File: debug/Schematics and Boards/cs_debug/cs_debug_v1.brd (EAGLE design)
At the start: 38.1 x 44.5 mm, 131 parts, among them J401 J-USB-HIROSE-MICRO-USB, Q10 2N7002P, Q3 FDN340P, Q4 2N7002P, Q5 FDN340P, Q6 2N7002P, Q7 FDN340P, Q8 2N7002P, Q9 FDN340P, U1 AP2120N-3.3TRG1, U10 OPA357AIDBVTG4, U2 TLV1117LV33DCYR, U3 INA225AIDGK, U4 OPA357AIDBVTG4, U5 INA225AIDGK, U6 OPA357AIDBVTG4, U7 INA225AIDGK, U8 OPA357AIDBVTG4, U9 INA225AIDGK, Y101 32.768kHz, Y102 12mHz-12pF-K7

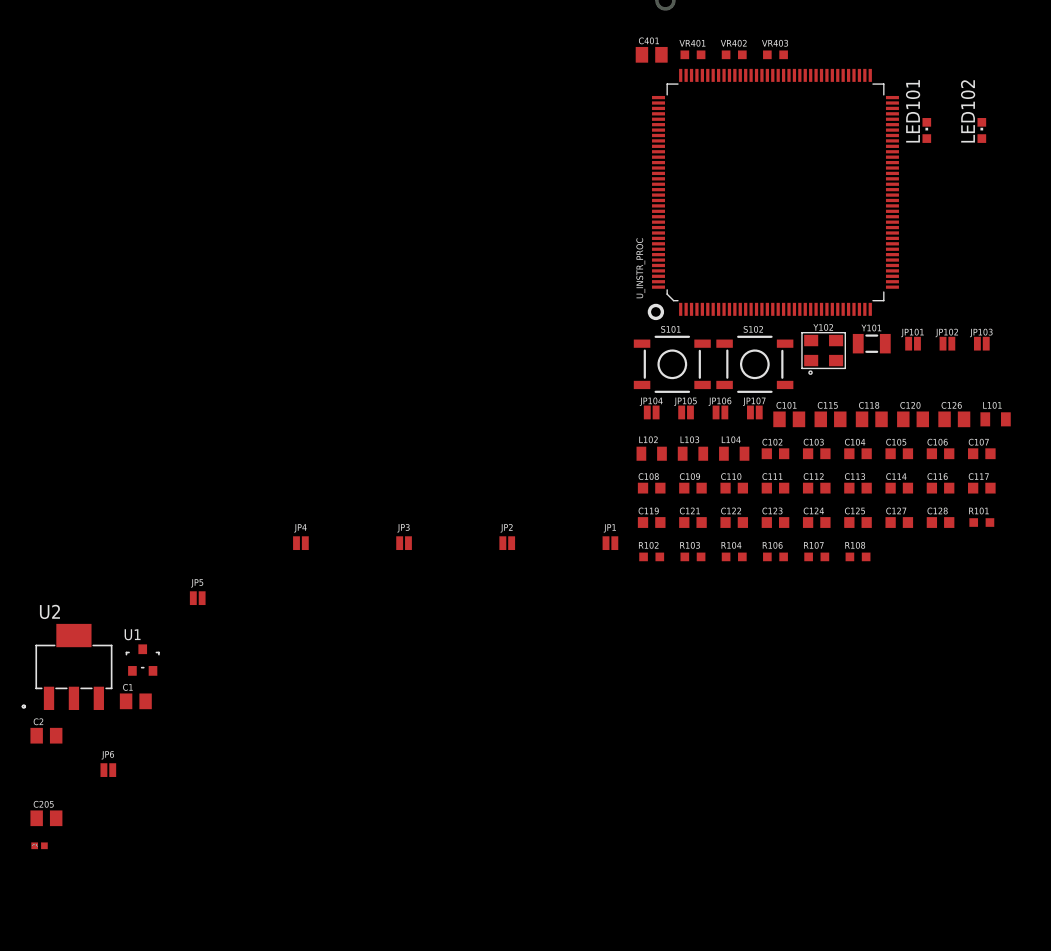
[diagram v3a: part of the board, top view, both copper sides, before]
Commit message: Signals from instrumentation processor to current monitors
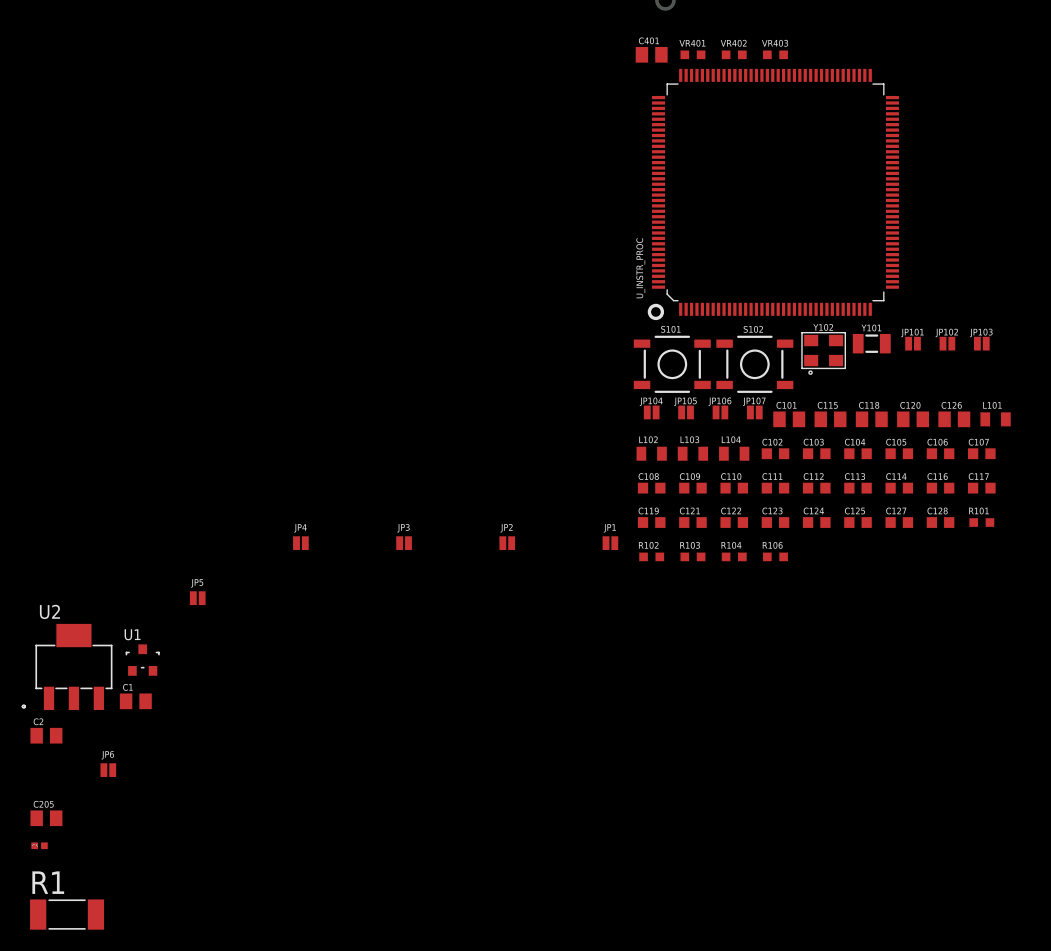
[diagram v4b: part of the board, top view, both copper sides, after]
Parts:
- removed LED101: RED, adafruit:CHIPLED_0603
- removed LED102: GREEN, adafruit:CHIPLED_0603
- removed R107, R108: 1k, Resistors:R0603
- added R1: 0, Resistors:R2010
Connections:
- net D+ renamed INSTR_PROC_USB_D_P
- net D- renamed INSTR_PROC_USB_D_N
- net MAIN_TRACE_D2 renamed MAIN_TRACE_D2/GPIO8
- net MAIN_TRACE_D3 renamed MAIN_TRACE_D3/GPIO9
- removed net CM_PROC_V_OFFSET_IN: R9.1
- removed net MAIN_TRACE_CLK: J_DEBUG_TO_MAIN_HEADER.26
- removed net MAIN_TRACE_D0: J_DEBUG_TO_MAIN_HEADER.23
- removed net MAIN_TRACE_D1: J_DEBUG_TO_MAIN_HEADER.25
- removed net MAIN_TRACE_SWO: J_DEBUG_TO_MAIN_HEADER.28
- removed net N$31: LED101.A, R107.1
- removed net USR_LED_GREEN: LED102.C
- removed net USR_LED_RED: LED101.C
- new net INSTR_PROC_USART_RX: U_INSTR_PROC.18
- new net INSTR_PROC_USART_TX: U_INSTR_PROC.17
- new net MAIN_TRACE_CLK/GPIO4: J_DEBUG_TO_MAIN_HEADER.26, U_INSTR_PROC.97
- new net MAIN_TRACE_D0/GPIO6: J_DEBUG_TO_MAIN_HEADER.23, U_INSTR_PROC.114
- new net MAIN_TRACE_D1/GPIO7: J_DEBUG_TO_MAIN_HEADER.25, U_INSTR_PROC.115
- new net MAIN_TRACE_SWO/GPIO5: J_DEBUG_TO_MAIN_HEADER.28, U_INSTR_PROC.113
- new net N$10: U_INSTR_PROC.87
- new net N$11: U_INSTR_PROC.85
- net 3V3_INSTR_PROC: no longer R107.2, R108.2
- net AGND: now also R1.2
- net CM_DTR_DCBIAS_SHUTDOWN: now also U_INSTR_PROC.15
- net CM_DTR_DIFFAMP_GAIN0: now also U_INSTR_PROC.64
- net CM_DTR_DIFFAMP_GAIN1: now also U_INSTR_PROC.63
- net CM_DTR_DIFFAMP_OUT: now also U_INSTR_PROC.82
- net CM_PROC_DCBIAS_SHUTDOWN: now also U_INSTR_PROC.16
- net CM_PROC_DIFFAMP_GAIN0: now also U_INSTR_PROC.66
- net CM_PROC_DIFFAMP_GAIN1: now also U_INSTR_PROC.65
- net CM_PROC_DIFFAMP_OUT: now also U_INSTR_PROC.78
- net CM_STORAGE_DCBIAS_SHUTDOWN: now also U_INSTR_PROC.14
- net CM_STORAGE_DIFFAMP_GAIN0: now also U_INSTR_PROC.116
- net CM_STORAGE_DIFFAMP_GAIN1: now also U_INSTR_PROC.60
- net CM_STORAGE_DIFFAMP_OUT: now also U_INSTR_PROC.83
- net CM_TEMP_DCBIAS_SHUTDOWN: now also U_INSTR_PROC.13
- net CM_TEMP_DIFFAMP_GAIN0: now also U_INSTR_PROC.59
- net CM_TEMP_DIFFAMP_GAIN1: now also U_INSTR_PROC.55
- net CM_TEMP_DIFFAMP_OUT: now also U_INSTR_PROC.84
- net DGND: now also R1.1
- net MAIN_GPIO0: now also U_INSTR_PROC.101
- net MAIN_GPIO1: now also U_INSTR_PROC.100
- net MAIN_GPIO2: now also U_INSTR_PROC.99
- net MAIN_GPIO3: now also U_INSTR_PROC.98
- net N$3: now also U_INSTR_PROC.129; no longer C205.1, C3.1, JP5.1, JP6.1
- net N$5: now also U_INSTR_PROC.86; no longer LED102.A, R108.1
- net VDD_TO_MAIN: now also C205.1, C3.1, JP5.1, JP6.1

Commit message: Add debug connectors, DAC, pull-ups to schematic
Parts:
- added C16: 0.1u, Capacitors:C0402
- added J1, J2: J-JTAG-CORTEX_SMD, Connectors:SAMTECH_FTSH-105-01
- added J3: J-JTAG-CORTEX-NEEDLE6-LEGS, Connectors:8.06.16_6-PIN_NEEDLE_ADAPTER_LEGS
- added JP7: JUMPER-SMT_2_NC_PASTE_NO-SILK, SparkFun-Jumpers:SMT-JUMPER_2_NC_PASTE_NO-SILK
- added R2, R3, R6: 100k, Resistors:R0402
- added R4, R5: 4.7k, Resistors:R0402
- added U11: DAC7574IDGS, DACs:DGS10
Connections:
- removed net CPU_RESET: C119.2, S101.3, S101.4, U_INSTR_PROC.47
- removed net N$10: U_INSTR_PROC.87
- removed net N$3: U_INSTR_PROC.129
- removed net N$5: U_INSTR_PROC.86
- removed net N$6: U_INSTR_PROC.28
- removed net N$7: U_INSTR_PROC.29
- removed net N$8: U_INSTR_PROC.30
- removed net N$9: U_INSTR_PROC.31
- removed net UOTGID: J401.USBID, VR401.1
- new net CM_PROC_V_OFFSET_IN: U11.1
- new net INSTR_PROC_I2C_SCL: R4.2, U11.6, U_INSTR_PROC.87
- new net INSTR_PROC_I2C_SDA: R5.2, U11.7, U_INSTR_PROC.86
- new net INSTR_PROC_JTAG_TCK/SWCLK: J2.4, J3.4, R3.1, U_INSTR_PROC.28
- new net INSTR_PROC_JTAG_TDI: J2.8, R6.1, U_INSTR_PROC.29
- new net INSTR_PROC_JTAG_TDO/SWO: J2.6, J3.6, U_INSTR_PROC.30
- new net INSTR_PROC_JTAG_TMS/SWDIO: J2.2, J3.2, R2.1, U_INSTR_PROC.31
- new net INSTR_PROC_NRESET: C119.2, J2.10, J3.3, S101.3, S101.4, U_INSTR_PROC.47
- new net INSTR_PROC_USB_UOTGID: J401.USBID, U_INSTR_PROC.129, VR401.1
- new net N$12: C205.1, C3.1, JP5.1, JP6.1, JP7.1
- net 3V3_INSTR_MEAS: now also C16.1, U11.8
- net 3V3_INSTR_PROC: now also J2.1, J3.1, R2.2, R3.2, R4.1, R5.1, R6.2
- net AGND: now also C16.2, U11.10, U11.3, U11.9
- net CM_DTR_V_OFFSET_IN: now also U11.2
- net CM_STORAGE_V_OFFSET_IN: now also U11.4
- net CM_TEMP_V_OFFSET_IN: now also U11.5
- net DGND: now also J1.3, J1.5, J2.3, J2.5, J2.9, J3.5
- net MAIN_NRESET: now also J1.10
- net MAIN_SWD_SWCLK: now also J1.4
- net MAIN_SWD_SWDIO: now also J1.2
- net VDD_TO_MAIN: now also JP7.2; no longer C205.1, C3.1, JP5.1, JP6.1
- net V_SENSE_P: now also J1.1

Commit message: Finish first-pass of Debug Board schematic
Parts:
- removed C101, C115, C118, C120, C126: 22uF, Capacitors:C0805
- removed C102, C106: 16pF, Capacitors:C0603
- removed C104, C105, C109, C110, C111, C112, C113, C114, C116, C117, C121, C122, C123, C124, C125, C127, C128: 0.1uF, Capacitors:C0603
- removed C119: 10nF, Capacitors:C0603
- removed R104, R106: 100k, Resistors:R0603
- removed S101: Momentary, Switches:TACTILE_SWITCH_SMD_5.2MM
- added C17, C19: 16pF, Capacitors:C0603
- added C18, C208: 4.7u, Capacitors:C0402
- added C20, C28: 10n, Capacitors:C0402
- added C21, C23, C24, C25, C26, C27: 22u, Capacitors:C0805
- added C22, C29, C30, C31, C32, C33, C34, C35, C36, C37, C38, C39, C40, C41, C42, C43, C44: 0.1u, Capacitors:C0402
- added D1: MBR120VLSFT3GOSCT-ND, adafruit:SOD-123
- added F2: MF-MSMF050-2, adafruit:1812
- added J19: Solar, Connectors:JST-PH-2-SMT-RA
- added JMP_LOG: (no value), Connectors:1X03
- added JP10: JUMPER-SMT_2_NC_PASTE_NO-SILK, SparkFun-Jumpers:SMT-JUMPER_2_NC_PASTE_NO-SILK
- added JP11: JUMPER-SMT_3_1-NC_PASTE_NO-SILK, Connectors:SMT-JUMPER_3_1-NC_PASTE_NO-SILK
- added JP12, JP8, JP9: JUMPER-SMT_2_NC_PASTE_NO-SILK, Connectors:SMT-JUMPER_2_NC_PASTE_NO-SILK
- added L1: 3.3µH/±20%/450mA, SparkFun-Coils:0805
- added R201: 270k, Resistors:R0402
- added R202, R204, R41, R8: 100k, Resistors:R0402
- added R203: 2k, Resistors:R0402
- added R206, R7: 10k, Resistors:R0402
- added S1: Momentary, Switches:SW_EVQ-P7L01P
- added S201: (no value), Switches:SWITCH_SPST_SMD_A
- added U12: MCP73871T-2CCI/ML, Chargers:QFN50P400X400X100-21N
- C401: device Capacitors:C0805 -> Capacitors:C0402
- R101, R102, R103: device Resistors:R0603 -> Resistors:R0402
- S102: device Switches:TACTILE_SWITCH_SMD_5.2MM -> Switches:SW_EVQ-P7L01P
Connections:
- removed net INSTR_PROC_USART_RX: U_INSTR_PROC.18
- removed net INSTR_PROC_USART_TX: U_INSTR_PROC.17
- removed net N$12: C205.1, C3.1, JP5.1, JP6.1, JP7.1
- removed net VUSB: C401.1, J401.VBUS
- new net BAT_CHG_PROG1: R203.2, U12.13
- new net CHG_VPCC: R201.1, R202.2, U12.2
- new net EXT_VIN: D1.A, J19.1
- new net GND: C18.2, C208.2, J19.2, S1.1_1, S1.1_2
- new net INSTR_PROC_NRESET_SW: C28.2, JP12.2, S1.2_1, S1.2_2, U_INSTR_PROC.47
- new net N$10: R204.2, U12.12
- new net N$3: JP8.2, U_INSTR_PROC.18
- new net N$5: JP9.2, U_INSTR_PROC.17
- new net N$6: L1.2, S201.2
- new net N$8: F2.2, U12.14, U12.15, U12.16
- new net THERM: R206.2, U12.5
- new net VCHRG_BATT: C18.1, F2.1, JP10.1
- new net VCHRG_OUT: C208.1, JP11.3, U12.1, U12.20
- new net VREG_IN: C205.1, C3.1, JP11.2, JP5.1, JP6.1, JP7.1
- new net VSRC_RAW: JP11.1, R201.2, S201.3, U12.17, U12.18, U12.19, U12.3, U12.4, U12.9
- net 3V3_INSTR_PROC: now also C27.1, C28.1, C37.1, C38.1, C39.1, C40.1, C41.1, C42.1, R41.1, S102.1_1, S102.1_2; no longer C101.1, C104.1, C105.1, C109.1, C110.1, C111.1, C112.1, C119.1, R106.2, S102.1, S102.2
- net ADVREF: now also C29.1; no longer C116.1
- net ADVREF_PRE: now also C22.1; no longer C114.1
- net CM_PROC_V_OFFSET_IN: now also R9.1
- net DGND: now also C17.2, C19.2, C20.2, C21.2, C22.2, C23.2, C24.2, C25.2, C26.2, C27.2, C29.2, C30.2, C31.2, C32.2, C33.2, C34.2, C35.2, C36.2, C37.2, C38.2, C39.2, C40.2, C41.2, C42.2, C43.2, C44.2, JMP_LOG.3, R202.1, R203.1, R204.1, R206.1, R7.1, R8.2, U12.10, U12.11, U12.21; no longer C101.2, C102.2, C104.2, C105.2, C106.2, C109.2, C110.2, C111.2, C112.2, C113.2, C114.2, C115.2, C116.2, C117.2, C118.2, C120.2, C121.2, C122.2, C123.2, C124.2, C125.2, C126.2, C127.2, C128.2, R104.1, S101.1, S101.2
- net ERASE_S: now also S102.2_1, S102.2_2; no longer S102.3, S102.4
- net FWUP: now also R41.2; no longer R106.1
- net INSTR_PROC_NRESET: now also JP12.1; no longer C119.2, S101.3, S101.4, U_INSTR_PROC.47
- net MAIN_USART_RX: now also JMP_LOG.1, JP8.1
- net MAIN_USART_TX: now also JMP_LOG.2, JP9.1
- net TST: now also R8.1; no longer R104.2
- net VBUS: now also C20.1, C21.1, C401.1, D1.C, J401.VBUS, L1.1, R7.2
- net VDDANA1: now also C25.1, C44.1; no longer C117.1, C118.1
- net VDDOUT: now also C23.1, C30.1, C31.1, C32.1, C33.1, C34.1, C35.1; no longer C120.1, C121.1, C122.1, C123.1, C125.1, C127.1, C128.1
- net VDDOUTMI: now also C26.1, C43.1; no longer C113.1, C115.1
- net VDDPLL: now also C24.1, C36.1; no longer C124.1, C126.1
- net V_BATT_MAIN: now also JP10.2
- net XIN: now also C19.1; no longer C106.1
- net XOUT: now also C17.1; no longer C102.1

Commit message: Change USART Header on debug board
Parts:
- removed JMP_LOG: (no value), Connectors:1X03
- added C45: 2.2uF, Capacitors:C0805
- added J4: J-SERIAL-PORT, Connectors:HEADER-1X6
- added J403: J-WURTH-USBC, Connectors:632723X00011
- added JP13: JUMPER-SMT_2_NC_PASTE_NO-SILK, Connectors:SMT-JUMPER_2_NC_PASTE_NO-SILK
- added R422, R423: 5.1k, Resistors:R0603
- added VR1, VR2: VARISTOR, Diodes:R0603
- moved R33 2.54 mm to (57.1, -48.9)
- moved R34 2.54 mm to (59.7, -48.9)
- moved R35 2.54 mm to (62.2, -48.9)
- moved R36 2.54 mm to (64.8, -48.9)
- moved R37 2.54 mm to (67.3, -48.9)
- moved C13 2.54 mm to (62.2, -46.4)
- moved C14 2.54 mm to (64.8, -46.4)
- moved C15 2.54 mm to (67.3, -46.4)
- moved Q10 2.54 mm to (58.4, -41.3)
- moved Q9 2.54 mm to (58.4, -36.2)
- moved R38 2.54 mm to (57.1, -51.4)
- moved R39 2.54 mm to (67.3, -40.0)
- moved R40 2.54 mm to (58.4, -46.4)
- moved U10 2.54 mm to (63.5, -42.5)
- moved U9 2.54 mm to (64.8, -36.2)
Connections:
- new net CC1: J403.A5, R422.2
- new net CC2: J403.B5, R423.2
- new net D+: J403.A6, J403.B6, VR1.1
- new net D-: J403.A7, J403.B7, VR2.1
- new net UCTX_DBGRX: J403.A8, J403.B8
- net 3V3_INSTR_PROC: now also JP13.1
- net DGND: now also J4.1; no longer JMP_LOG.3
- net GND: now also C45.2, J403.A1, J403.A12, J403.B1, J403.B12, J403.GND, J403.GND1, J403.Z1, J403.Z2, J403.Z3, J403.Z4, J403.Z5, J403.Z6, R422.1, R423.1, VR1.2, VR2.2
- net MAIN_USART_RX: now also J4.5; no longer JMP_LOG.1
- net MAIN_USART_TX: now also J4.4; no longer JMP_LOG.2
- net N$11: now also J4.3, JP13.2; no longer U_INSTR_PROC.85
- net VBUS: now also C45.1, J403.A4, J403.A9, J403.B4, J403.B9

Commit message: Add USB connector and switch IC
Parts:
- removed C20: 10n, Capacitors:C0402
- removed C21: 22u, Capacitors:C0805
- removed C401: 2.2uF, Capacitors:C0402
- removed C45: 2.2uF, Capacitors:C0805
- removed J401: J-USB-HIROSE-MICRO-USB, Connectors:USB-THRU-ZX62D-AB-5P8
- removed J403: J-WURTH-USBC, Connectors:632723X00011
- removed R422, R423: 5.1k, Resistors:R0603
- removed R7: 10k, Resistors:R0402
- removed VR1, VR2, VR401, VR402, VR403: VARISTOR, Diodes:R0603
- added C46: 2.2uF, Capacitors:C0805
- added C47: 1u, Capacitors:C0402
- added C48, C49, C50, C51, C52, C53: 0.1u, Capacitors:C0402
- added C54: 4.7u, Capacitors:C0402
- added C55, C56: 18pF, Capacitors:C0402
- added J5: J-WURTH-USBC, Connectors:632723X00011
- added JP14, JP15, JP16: JUMPER-SMT_2_NC_PASTE_NO-SILK, SparkFun-Jumpers:SMT-JUMPER_2_NC_PASTE_NO-SILK
- added L2: DLP11SN900HL2L, Inductors:IND_DLP11S_0504_MUR
- added R42, R43: 5.1k, Resistors:R0603
- added R44, R45, R51, R52: 10k, Resistors:R0402
- added R46, R47, R49, R50: 100k, Resistors:R0402
- added R48: 12k, Resistors:R0402
- added U$5: BGX50A, Diodes:SOT143_BGX50A
- added U13: USB2412-DZK, Switches:QFN28_5X5MC_MCH
- added VR3, VR4: VARISTOR, Diodes:R0603
- added Y1: HCM49-24.000MABJ-UT, Oscillators:XTAL_HCM49
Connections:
- removed net CC1: J403.A5, R422.2
- removed net CC2: J403.B5, R423.2
- removed net D+: J403.A6, J403.B6, VR1.1
- removed net D-: J403.A7, J403.B7, VR2.1
- removed net VBUS: C20.1, C21.1, C401.1, C45.1, D1.C, J401.VBUS, J403.A4, J403.A9, J403.B4, J403.B9, L1.1, R7.2, U_INSTR_PROC.39
- new net CC3: J5.A5, R42.2
- new net CC4: J5.B5, R43.2
- new net N$12: U13.15, U13.6
- new net N$14: R45.1, U13.7
- new net N$15: D1.C, JP14.1
- new net N$16: R44.1, U13.11
- new net N$17: R48.2, U13.26
- new net N$18: R46.2, R47.1, U13.18
- new net N$19: C48.1, R49.1, U13.17
- new net N$20: C55.1, U13.24, Y1.1
- new net N$21: C56.1, U13.23, Y1.2
- new net N$22: R50.2, U13.16
- new net N$23: R52.1, U13.13
- new net N$24: R51.1, U13.19
- new net USB_CONN_D_N: J5.A6, J5.B6, L2.3, U$5.2, VR3.1
- new net USB_CONN_D_P: J5.A7, J5.B7, L2.2, U$5.4, VR4.1
- new net USB_D_N: L2.4, U13.21
- new net USB_D_P: L2.1, U13.22
- new net USB_VBUS: C46.1, C47.1, J5.A4, J5.A9, J5.B4, J5.B9, JP14.2, JP15.1, JP15.2, L1.1, R47.2, U$5.1, U_INSTR_PROC.39
- net 3V3_INSTR_PROC: now also C49.1, C50.1, C51.1, C52.1, C53.1, C54.1, R44.2, R45.2, R49.2, R51.2, R52.2, U13.10, U13.14, U13.20, U13.27, U13.4
- net DGND: now also C46.2, C47.2, C48.2, C49.2, C50.2, C51.2, C52.2, C53.2, C54.2, C55.2, C56.2, J5.A1, J5.A12, J5.B1, J5.B12, J5.GND, J5.GND1, J5.Z1, J5.Z2, J5.Z3, J5.Z4, J5.Z5, J5.Z6, R42.1, R43.1, R46.1, R48.1, R50.1, U$5.3, U13.29, VR3.2, VR4.2; no longer C20.2, C21.2, C401.2, J401.GND, J401.S1, J401.S2, J401.S3, J401.S4, R7.1, VR401.2, VR402.2, VR403.2
- net GND: no longer C45.2, J403.A1, J403.A12, J403.B1, J403.B12, J403.GND, J403.GND1, J403.Z1, J403.Z2, J403.Z3, J403.Z4, J403.Z5, J403.Z6, R422.1, R423.1, VR1.2, VR2.2
- net INSTR_PROC_USB_D_N: now also U13.2; no longer J401.D-, VR403.1
- net INSTR_PROC_USB_D_P: now also U13.3; no longer J401.D+, VR402.1
- net INSTR_PROC_USB_UOTGID: no longer J401.USBID, VR401.1
- net MAIN_USART_TX: now also JP16.2
- net MAIN_USB_DATA_N: now also U13.28
- net MAIN_USB_DATA_P: now also U13.1
- net UCTX_DBGRX: now also J5.A8, J5.B8, JP16.1; no longer J403.A8, J403.B8
